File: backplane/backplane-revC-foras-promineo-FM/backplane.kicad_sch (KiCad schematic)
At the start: 32 parts, among them J101 BURN WIRES, J103 SEP1 & SEP2, J104 SEP3 & SEP4, J105 +X SOLAR PANEL, J106 -X SOLAR PANEL, J107 +Y SOLAR PANEL, J108 -Z SOLAR PANEL, J200_1 HSEC8-160-01-S-DV-A-K-TR, J200_2 HSEC8-160-01-S-DV-A-K-TR, J200_3 HSEC8-160-01-S-DV-A-K-TR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

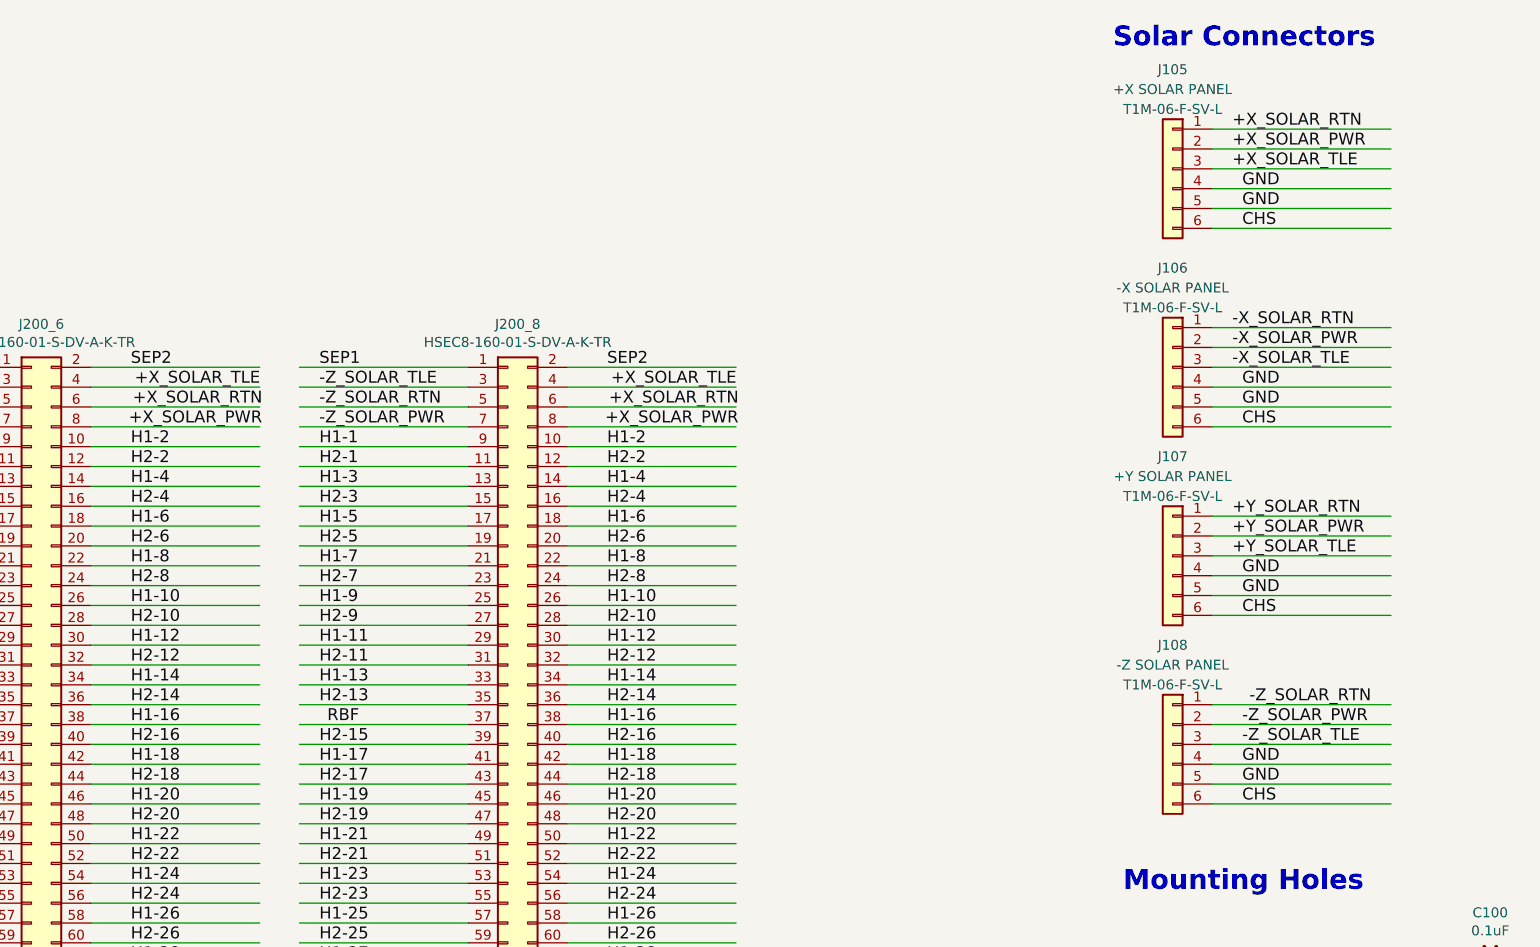
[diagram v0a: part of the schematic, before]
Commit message: Fixed pinout of solar panel connectors on backplane
pinout didnt match solar panels. pins 7 and 8 on solar panels aren't used. pin 7 is an extra tlm connection, pin 8 is an extra chs connection.
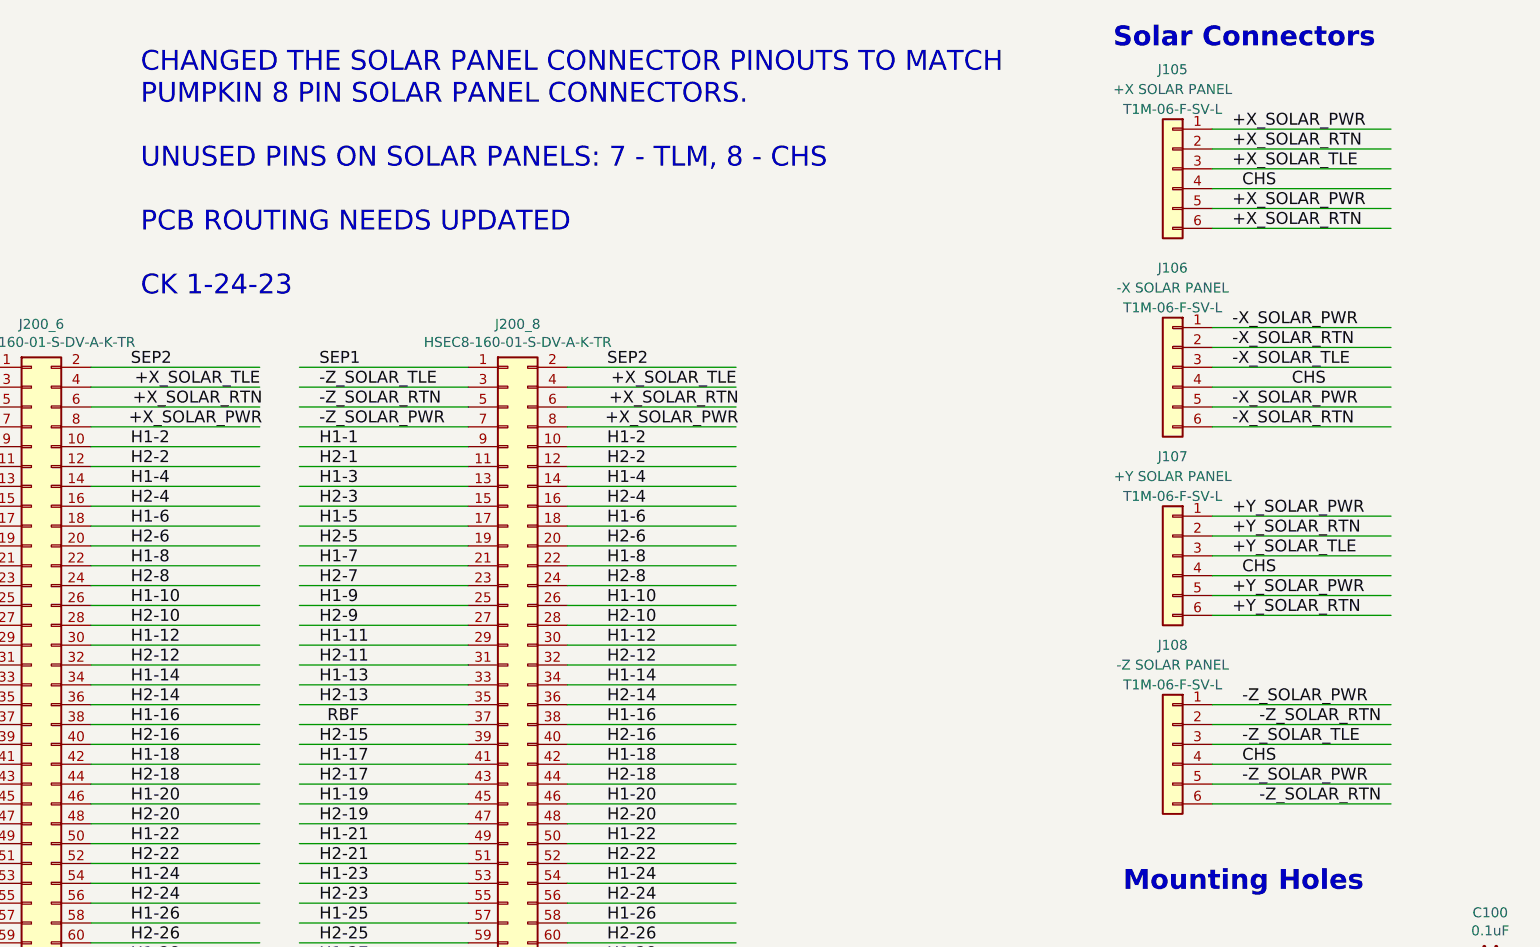
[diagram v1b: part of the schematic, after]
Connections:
- net +X_SOLAR_PWR: now also J105.1 (Pin_1), J105.5 (Pin_5); no longer J105.2 (Pin_2)
- net +X_SOLAR_RTN: now also J105.2 (Pin_2), J105.6 (Pin_6); no longer J105.1 (Pin_1)
- net +Y_SOLAR_PWR: now also J107.1 (Pin_1), J107.5 (Pin_5); no longer J107.2 (Pin_2)
- net +Y_SOLAR_RTN: now also J107.2 (Pin_2), J107.6 (Pin_6); no longer J107.1 (Pin_1)
- net -X_SOLAR_PWR: now also J106.1 (Pin_1), J106.5 (Pin_5); no longer J106.2 (Pin_2)
- net -X_SOLAR_RTN: now also J106.2 (Pin_2), J106.6 (Pin_6); no longer J106.1 (Pin_1)
- net -Z_SOLAR_PWR: now also J108.1 (Pin_1), J108.5 (Pin_5); no longer J108.2 (Pin_2)
- net -Z_SOLAR_RTN: now also J108.2 (Pin_2), J108.6 (Pin_6); no longer J108.1 (Pin_1)
- net CHS: now also J105.4 (Pin_4), J106.4 (Pin_4), J107.4 (Pin_4), J108.4 (Pin_4); no longer J105.6 (Pin_6), J106.6 (Pin_6), J107.6 (Pin_6), J108.6 (Pin_6)
- net GND: no longer J105.4 (Pin_4), J105.5 (Pin_5), J106.4 (Pin_4), J106.5 (Pin_5), J107.4 (Pin_4), J107.5 (Pin_5), J108.4 (Pin_4), J108.5 (Pin_5)
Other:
- note added: "CHANGED THE SOLAR PANEL CONNECTOR PINOUTS TO MATCH PUMPKIN 8 PIN SOLAR PANEL CONNECTORS. UNUSED PINS ON SOLAR PANELS: 7 - TLM, 8 - CHS PCB ROUTING NEEDS UPDATED CK 1-24-23"
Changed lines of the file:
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@@
     (effects (font (size 2.54 2.54) (thickness 0.508) bold) (justify left bottom))
   )
+  (text "CHANGED THE SOLAR PANEL CONNECTOR PINOUTS TO MATCH \nPUMPKIN 8 PIN SOLAR PANEL CONNECTORS. \n\nUNUSED PINS ON SOLAR PANELS: 7 - TLM, 8 - CHS\n\nPCB ROUTING NEEDS UPDATED\n\nCK 1-24-23"
+    (at 191.77 52.07 0)
+    (effects (font (size 2.54 2.54)) (justify left bottom))
+  )
   (text "BACKPLANE BREAKOUT CONNECTOR IS \nONLY USED FOR GROUND TESTING\nCONTACT RATING 2.1A PER PIN  \nTRACE WIDTH: 0.25mm \nVIA SIZE: 0.2mm DRILL, 0.5mm PAD"
     (at 467.36 314.96 0)
@@
     (effects (font (size 1.524 1.524)) (justify left bottom))
   )
-  (label "GND" (at 332.74 111.76 0)
-    (effects (font (size 1.524 1.524)) (justify left bottom))
-  )
   (label "H2-33" (at 214.63 154.94 0)
     (effects (font (size 1.524 1.524)) (justify left bottom))
@@
     (effects (font (size 1.524 1.524)) (justify left bottom))
   )
-  (label "GND" (at 332.74 66.04 0)
-    (effects (font (size 1.524 1.524)) (justify left bottom))
-  )
   (label "H2-43" (at 31.75 180.34 0)
     (effects (font (size 1.524 1.524)) (justify left bottom))
@@
     (effects (font (size 1.524 1.524)) (justify left bottom))
   )
-  (label "GND" (at 332.74 114.3 0)
-    (effects (font (size 1.524 1.524)) (justify left bottom))
-  )
   (label "H2-45" (at 31.75 349.25 0)
     (effects (font (size 1.524 1.524)) (justify left bottom))
@@
     (effects (font (size 1.524 1.524)) (justify left bottom))
   )
-  (label "CHS" (at 332.74 116.84 0)
+  (label "CHS" (at 332.74 111.76 0)
     (effects (font (size 1.524 1.524)) (justify left bottom))
   )
@@
     (effects (font (size 1.524 1.524)) (justify left bottom))
   )
-  (label "CHS" (at 332.74 92.71 0)
-    (effects (font (size 1.524 1.524)) (justify left bottom))
-  )
   (label "SEP3" (at 92.71 210.82 0)
     (effects (font (size 1.524 1.524)) (justify left bottom))
@@
     (effects (font (size 1.524 1.524)) (justify left bottom))
   )
-  (label "GND" (at 332.74 38.1 0)
+  (label "CHS" (at 332.74 38.1 0)
     (effects (font (size 1.524 1.524)) (justify left bottom))
   )
@@
     (effects (font (size 1.524 1.524)) (justify left bottom))
   )
+  (label "CHS" (at 332.74 87.63 0)
+    (effects (font (size 1.524 1.524)) (justify left bottom))
+  )
   (label "H1-46" (at 67.31 346.71 0)
     (effects (font (size 1.524 1.524)) (justify left bottom))
@@
     (effects (font (size 1.524 1.524)) (justify left bottom))
   )
+  (label "+Y_SOLAR_PWR" (at 331.47 90.17 0)
+    (effects (font (size 1.524 1.524)) (justify left bottom))
+  )
   (label "H1-33" (at 153.67 152.4 0)
     (effects (font (size 1.524 1.524)) (justify left bottom))
@@
     (effects (font (size 1.524 1.524)) (justify left bottom))
   )
-  (label "+X_SOLAR_PWR" (at 331.47 33.02 0)
+  (label "+X_SOLAR_PWR" (at 331.47 30.48 0)
     (effects (font (size 1.524 1.524)) (justify left bottom))
   )
@@
     (effects (font (size 1.524 1.524)) (justify left bottom))
   )
-  (label "-Z_SOLAR_PWR" (at 332.74 106.68 0)
+  (label "-Z_SOLAR_PWR" (at 332.74 104.14 0)
     (effects (font (size 1.524 1.524)) (justify left bottom))
   )
@@
     (effects (font (size 1.524 1.524)) (justify left bottom))
   )
+  (label "-Z_SOLAR_PWR" (at 332.74 114.3 0)
+    (effects (font (size 1.524 1.524)) (justify left bottom))
+  )
   (label "-Z_SOLAR_RTN" (at 214.63 66.04 0)
     (effects (font (size 1.524 1.524)) (justify left bottom))
@@
     (effects (font (size 1.524 1.524)) (justify left bottom))
   )
-  (label "-X_SOLAR_PWR" (at 331.47 58.42 0)
+  (label "-X_SOLAR_PWR" (at 331.47 55.88 0)
     (effects (font (size 1.524 1.524)) (justify left bottom))
   )
@@
     (effects (font (size 1.524 1.524)) (justify left bottom))
   )
-  (label "GND" (at 332.74 90.17 0)
-    (effects (font (size 1.524 1.524)) (justify left bottom))
-  )
   (label "H2-40" (at 128.27 170.18 0)
     (effects (font (size 1.524 1.524)) (justify left bottom))
   )
-  (label "CHS" (at 332.74 43.18 0)
+  (label "+X_SOLAR_RTN" (at 331.47 43.18 0)
     (effects (font (size 1.524 1.524)) (justify left bottom))
   )
@@
     (effects (font (size 1.524 1.524)) (justify left bottom))
   )
-  (label "GND" (at 332.74 40.64 0)
-    (effects (font (size 1.524 1.524)) (justify left bottom))
-  )
   (label "H1-34" (at 189.23 316.23 0)
     (effects (font (size 1.524 1.524)) (justify left bottom))
@@
     (effects (font (size 1.524 1.524)) (justify left bottom))
   )
+  (label "-Z_SOLAR_RTN" (at 350.52 106.68 180)
+    (effects (font (size 1.524 1.524)) (justify right bottom))
+  )
   (label "SEP1" (at 153.67 60.96 0)
     (effects (font (size 1.524 1.524)) (justify left bottom))
@@
     (effects (font (size 1.524 1.524)) (justify left bottom))
   )
-  (label "GND" (at 332.74 63.5 0)
-    (effects (font (size 1.524 1.524)) (justify left bottom))
-  )
   (label "H2-50" (at 508 279.4 0)
     (effects (font (size 1.524 1.524)) (justify left bottom))
@@
     (effects (font (size 1.524 1.524)) (justify left bottom))
   )
+  (label "-X_SOLAR_RTN" (at 331.47 68.58 0)
+    (effects (font (size 1.524 1.524)) (justify left bottom))
+  )
   (label "USER_2" (at 30.988 356.87 0)
     (effects (font (size 1.524 1.524)) (justify left bottom))
@@
     (effects (font (size 1.524 1.524)) (justify left bottom))
   )
-  (label "-Z_SOLAR_RTN" (at 349.25 104.14 180)
+  (label "-Z_SOLAR_RTN" (at 350.52 116.84 180)
     (effects (font (size 1.524 1.524)) (justify right bottom))
   )
@@
     (effects (font (size 1.524 1.524)) (justify left bottom))
   )
-  (label "+Y_SOLAR_PWR" (at 331.47 82.55 0)
+  (label "+Y_SOLAR_PWR" (at 331.47 80.01 0)
     (effects (font (size 1.524 1.524)) (justify left bottom))
   )
@@
     (effects (font (size 1.524 1.524)) (justify left bottom))
   )
+  (label "+X_SOLAR_PWR" (at 331.47 40.64 0)
+    (effects (font (size 1.524 1.524)) (justify left bottom))
+  )
   (label "H2-40" (at 128.27 334.01 0)
     (effects (font (size 1.524 1.524)) (justify left bottom))
@@
     (effects (font (size 1.524 1.524)) (justify left bottom))
   )
-  (label "GND" (at 332.74 87.63 0)
-    (effects (font (size 1.524 1.524)) (justify left bottom))
-  )
   (label "H1-9" (at 31.75 255.27 0)
     (effects (font (size 1.524 1.524)) (justify left bottom))
@@
     (effects (font (size 1.524 1.524)) (justify left bottom))
   )
+  (label "-X_SOLAR_PWR" (at 331.47 66.04 0)
+    (effects (font (size 1.524 1.524)) (justify left bottom))
+  )
   (label "H2-50" (at 67.31 195.58 0)
     (effects (font (size 1.524 1.524)) (justify left bottom))
@@
     (effects (font (size 1.524 1.524)) (justify left bottom))
   )
-  (label "-X_SOLAR_RTN" (at 331.47 55.88 0)
+  (label "-X_SOLAR_RTN" (at 331.47 58.42 0)
     (effects (font (size 1.524 1.524)) (justify left bottom))
   )
@@
     (effects (font (size 1.524 1.524)) (justify left bottom))
   )
-  (label "CHS" (at 332.74 68.58 0)
+  (label "CHS" (at 339.09 63.5 0)
     (effects (font (size 1.524 1.524)) (justify left bottom))
   )
@@
     (effects (font (size 1.524 1.524)) (justify left bottom))
   )
+  (label "+Y_SOLAR_RTN" (at 331.47 92.71 0)
+    (effects (font (size 1.524 1.524)) (justify left bottom))
+  )
   (label "GND" (at 68.326 144.78 0)
     (effects (font (size 1.524 1.524)) (justify left bottom))
@@
     (effects (font (size 1.524 1.524)) (justify left bottom))
   )
-  (label "+X_SOLAR_RTN" (at 331.47 30.48 0)
+  (label "+X_SOLAR_RTN" (at 331.47 33.02 0)
     (effects (font (size 1.524 1.524)) (justify left bottom))
   )
@@
     (effects (font (size 1.524 1.524)) (justify left bottom))
   )
-  (label "+Y_SOLAR_RTN" (at 331.47 80.01 0)
+  (label "+Y_SOLAR_RTN" (at 331.47 82.55 0)
     (effects (font (size 1.524 1.524)) (justify left bottom))
   )

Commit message: added rbf_ret net, added capability for neopixels on BP cards, added jumpers to bypass this
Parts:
- added R604 (x8): 0R, Resistor_SMD:R_0402_1005Metric, symbol backplane-rescue:R_US-Device
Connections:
- removed net H2-46: J200_1.100 (Pin_100), J200_2.100 (Pin_100), J200_3.100 (Pin_100), J200_4.100 (Pin_100), J200_5.100 (Pin_100), J200_6.100 (Pin_100), J200_7.100 (Pin_100), J200_8.100 (Pin_100), J301.50 (Pin_50)
- net H2-49 renamed RBF_RET
- removed net USER_1: J200_1.102 (Pin_102), J200_2.102 (Pin_102), J200_3.102 (Pin_102), J200_4.102 (Pin_102), J200_5.102 (Pin_102), J200_6.102 (Pin_102), J200_7.102 (Pin_102), J200_8.102 (Pin_102), J300.52 (Pin_52)
- net USER_2 renamed BP_LED_PWR
- net USER_3 renamed ~{BP_LED_EN}
- new net DIN_BO_LED: J301.50 (Pin_50), R604.2
- new net DIN_BP_LED: J200_8.102 (Pin_102)
- new net DIN_LED_1: J200_1.100 (Pin_100), J300.52 (Pin_52), R604.1, R604.2
- new net DIN_LED_2: J200_1.102 (Pin_102), J200_2.100 (Pin_100), R604.1, R604.2
- new net DIN_LED_3: J200_2.102 (Pin_102), J200_3.100 (Pin_100), R604.1, R604.2
- new net DIN_LED_4: J200_3.102 (Pin_102), J200_4.100 (Pin_100), R604.1, R604.2
- new net DIN_LED_5: J200_4.102 (Pin_102), J200_5.100 (Pin_100), R604.1, R604.2
- new net DIN_LED_6: J200_5.102 (Pin_102), J200_6.100 (Pin_100), R604.1, R604.2
- new net DIN_LED_7: J200_6.102 (Pin_102), J200_7.100 (Pin_100), R604.1, R604.2
- new net DIN_LED_8: J200_7.102 (Pin_102), J200_8.100 (Pin_100), R604.1
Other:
- sheet LED Driver ports: added DOUT, GND, LED_PWR, ~{LED_EN}; removed 5V_USB
- note added: "DIN_LED-DOUT_LED jumpers install when not used per backplane connector."
- note added: "DNP"
- note removed: "CHANGED THE SOLAR PANEL CONNECTOR PINOUTS TO MATCH PUMPKIN 8 PIN SOLAR PANEL CONNECTORS. UNUSED PINS ON SOLAR PANELS: 7 - TLM, 8 - CHS PCB ROUTING NEEDS UPDATED CK 1-24-23"
- note removed: "LED Driver"
- note removed: "SIN and SCLK are connected to the SDO0 and SCK0 pins on the bus respectively USER_1 (active high) not only activates the latch on U600-601 but allows serial data to pass to them"
- moved on the sheet: R100
